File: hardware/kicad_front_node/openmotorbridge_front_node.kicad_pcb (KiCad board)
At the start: 2 copper layers, 82 x 50 mm, 54 parts, among them J1 12V_KL15_GND, J10 12V_QI_POWER, J11 12V_AUX_LIGHT, J12 QWIIC_I2C, J2 CAN_H_L_GND, J3 HANDLEBAR_MULTI_BTN, J4 USB_UPSTREAM_HOST, J5 USB_DN1_PHONE_PD20W, J5_MP3 USB_DN3_GLOVEBOX_PD20W, J6 USB_DN2_CP2AA_PIGTAIL, J6_AUX USB_DN4_COCKPIT_AUX, J7 USB-C_SERVICE, J8 ACTION_CAM_5V_PWR, J9 MIRROR_BSD_LEDS, K1 CPC1017N_CAN_RELAY, Q1 DMN63D8_BSD_MOSFET, Q2 TPS1H100_AUX_LIGHT, SW1 BOOT, SW2 RESET, U1 ESP32-S3-WROOM-1U, U2 USB2514Bi-AEZG, U3 TPS54302_5V_BUCK, U4 TPS2051B_PORT2_GATE, U5 SW3526_USB_PD1_20W, U6 TCAN334G_CAN, U7 TLV75533P_3V3_LDO, U8 SW3526_USB_PD3_20W, Y1 24.000MHz

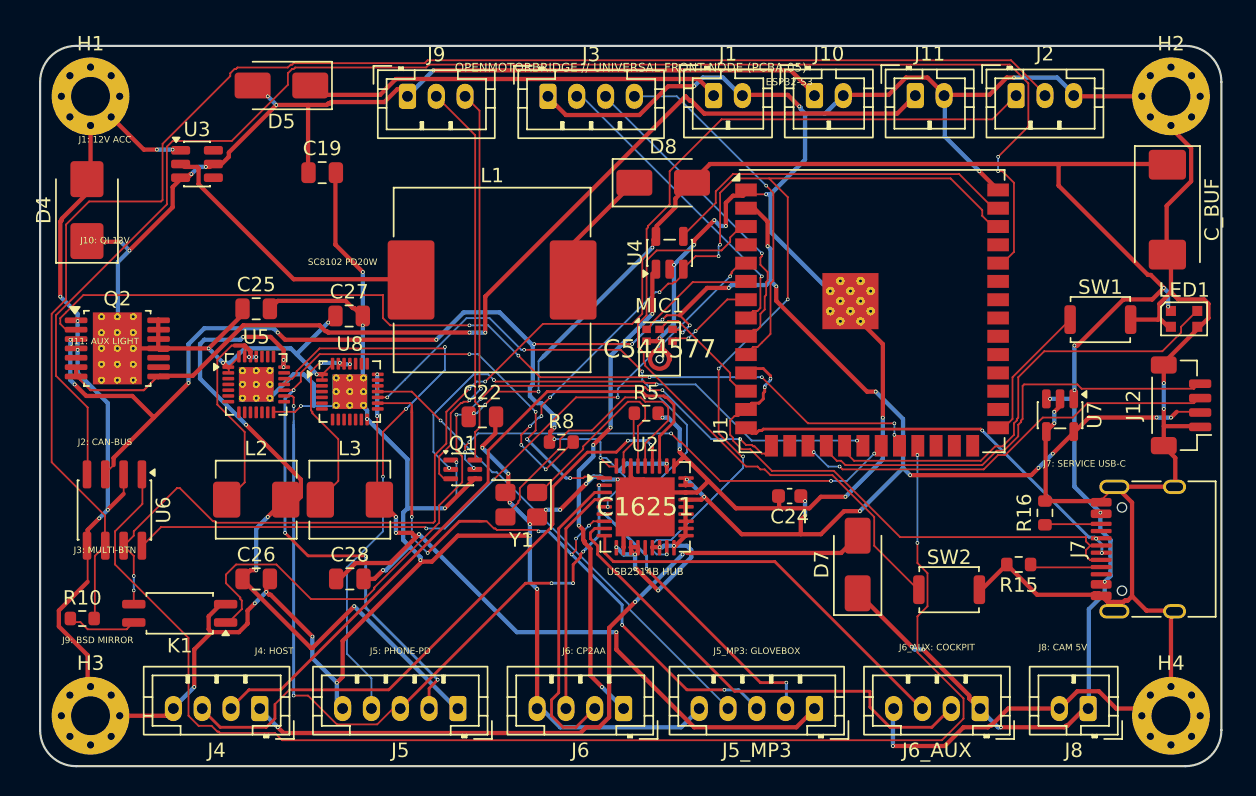
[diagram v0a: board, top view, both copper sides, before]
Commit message: hardware(pcb): mathematically align edge connectors on Front Node (PCBA 05) and Pod Cartridge (PCBA 03)
- Front Node top edge: align J1, J10, J11, J2, J3, J9 to consistent Y=73.500 (fixing 50µm step) and harmonize J9-J3 clearance to 1.60 mm
- Front Node bottom edge: adjust J5 and J6 by 0.25 mm so all 6 USB/cam ports have exactly 1.600 mm clearance
- Front Node right edge: smooth J7 USB-C service port to clean 0.5 mm grid at Y=105.000
- Pod Cartridge: smooth J_ACT to X=132.000 (3.00 mm distance to edge)
- Add inspect_and_align_pcb_connectors.py diagnostic and alignment tool
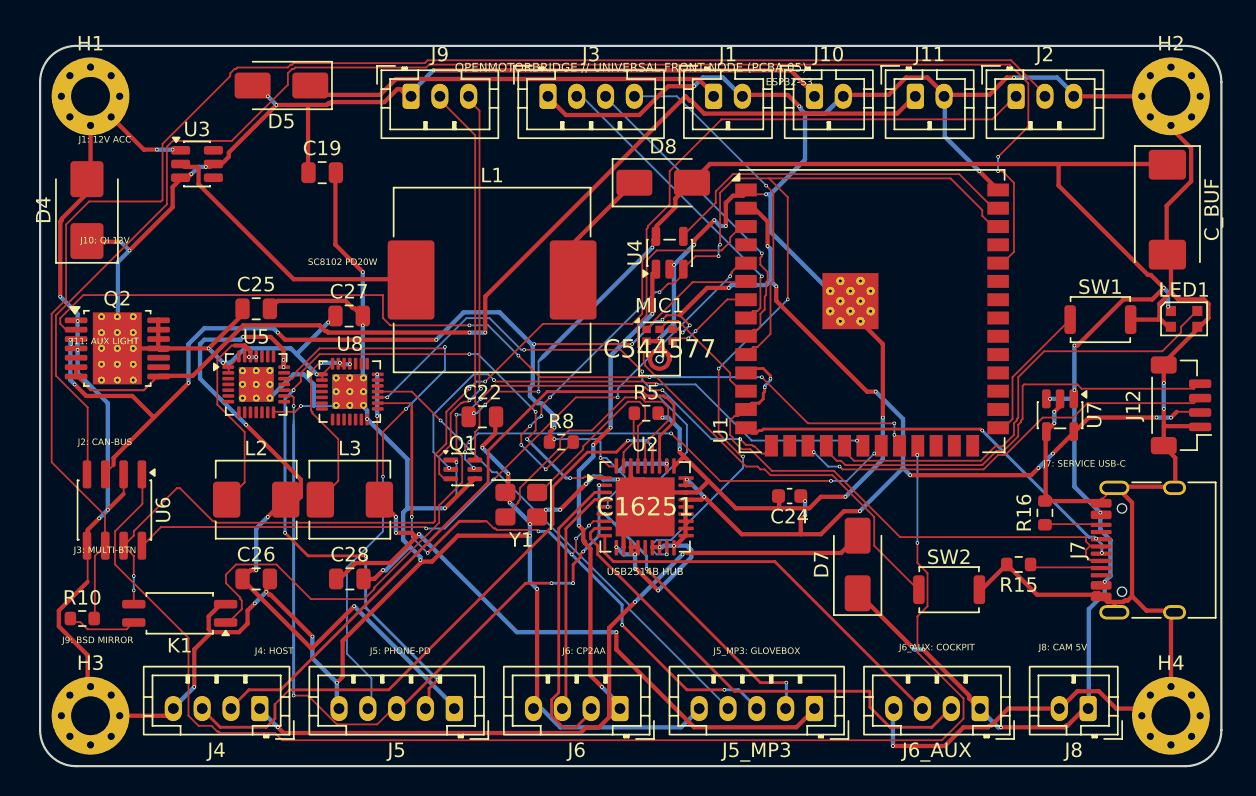
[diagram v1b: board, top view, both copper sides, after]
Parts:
- moved J5 0.25 mm to (128.8, 116.0)
- moved J6 0.25 mm to (140.2, 116.0)
- moved J9 0.25 mm to (125.8, 73.5)
- moved J7 0.07 mm to (177.7, 105.0)
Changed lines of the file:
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@@
 	(footprint "JST_PH_B5B-PH-K_1x05_P2.00mm_Vertical"
 		(layer "F.Cu")
-		(at 129 116 180)
+		(at 128.750 116.000 180.0)
 		(descr "JST PH series connector, B5B-PH-K (http://www.jst-mfg.com/product/pdf/eng/ePH.pdf)")
 		(tags "connector JST PH vertical")
@@
 	(footprint "JST_PH_B2B-PH-K_1x02_P2.00mm_Vertical"
 		(layer "F.Cu")
-		(at 153.75 73.45)
+		(at 153.750 73.500)
 		(descr "JST PH series connector, B2B-PH-K (http://www.jst-mfg.com/product/pdf/eng/ePH.pdf)")
 		(tags "connector JST PH vertical")
@@
 	(footprint "JST_PH_B3B-PH-K_1x03_P2.00mm_Vertical"
 		(layer "F.Cu")
-		(at 125.5 73.5)
+		(at 125.750 73.500)
 		(descr "JST PH series connector, B3B-PH-K (http://www.jst-mfg.com/product/pdf/eng/ePH.pdf)")
 		(tags "connector JST PH vertical")
@@
 	(footprint "JST_PH_B2B-PH-K_1x02_P2.00mm_Vertical"
 		(layer "F.Cu")
-		(at 146.75 73.45)
+		(at 146.750 73.500)
 		(descr "JST PH series connector, B2B-PH-K (http://www.jst-mfg.com/product/pdf/eng/ePH.pdf)")
 		(tags "connector JST PH vertical")
@@
 	(footprint "JST_PH_B2B-PH-K_1x02_P2.00mm_Vertical"
 		(layer "F.Cu")
-		(at 160.75 73.45)
+		(at 160.750 73.500)
 		(descr "JST PH series connector, B2B-PH-K (http://www.jst-mfg.com/product/pdf/eng/ePH.pdf)")
 		(tags "connector JST PH vertical")
@@
 	(footprint "JST_PH_B4B-PH-K_1x04_P2.00mm_Vertical"
 		(layer "F.Cu")
-		(at 140.5 116 180)
+		(at 140.250 116.000 180.0)
 		(descr "JST PH series connector, B4B-PH-K (http://www.jst-mfg.com/product/pdf/eng/ePH.pdf)")
 		(tags "connector JST PH vertical")
@@
 	(footprint "USB_C_Receptacle_HRO_TYPE-C-31-M-12"
 		(layer "F.Cu")
-		(at 177.7 104.93 90)
+		(at 177.700 105.000 90.0)
 		(descr "USB Type-C receptacle for USB 2.0 and PD, http://www.krhro.com/uploads/soft/180320/1-1P320120243.pdf")
 		(tags "usb usb-c 2.0 pd")
@@
 	(footprint "JST_PH_B3B-PH-K_1x03_P2.00mm_Vertical"
 		(layer "F.Cu")
-		(at 167.75 73.45)
+		(at 167.750 73.500)
 		(descr "JST PH series connector, B3B-PH-K (http://www.jst-mfg.com/product/pdf/eng/ePH.pdf)")
 		(tags "connector JST PH vertical")

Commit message: hardware(pcb): synchronize 5-PCBA lineup with v9.6 All-UWB architecture
- PCBA 01 (Central Box): replace obsolete 26-pin IDC header with 12-pin Deutsch DTM-12 header (exact 12-pin net mapping), add 38.4MHz UWB crystal on B.Cu, update silkscreen and schematic
- PCBA 05 (Front Node): place Qorvo DW3110 + U.FL + crystal on B.Cu; place u-blox SAM-M10Q GNSS + Knowles MEMS mic on F.Cu
- PCBA 03 (Pod Cartridge): replace obsolete 6-pin dock socket with PAD1/PAD2 DC spring contact pads; place DW3110 + U.FL on B.Cu
- PCBA 08 (Radar Sub-MCU): update J1 to 2-pin 12V automotive power connector; place DW3110 + U.FL on B.Cu
- PCBA 07 (Smart Keyfob): replace solder pads with 2-pin JST-ACH SMD header (J_QI) for solderless Qi coil connection
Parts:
- added ANT_UWB: Taoglas_FXUWB10, Connector_Coaxial:U.FL_Hirose_U.FL-R-SMT-1_Vertical, B.Cu at (137.0, 95.0)
- added MK1: SPH0645LM4H, Sensor_Audio:Knowles_SPH0645LM4H, F.Cu at (175.0, 85.0)
- added U10: u-blox_SAM-M10Q, RF_GPS:ublox_SAM-M10Q, F.Cu at (125.0, 85.0)
- added U9: DW3110, Package_DFN_QFN:QFN-16-1EP_3x3mm_P0.5mm_EP1.7x1.7mm_ThermalVias, B.Cu at (145.0, 95.0)
- added Y_UWB: 38.4MHz, Crystal:Crystal_SMD_2016-4Pin_2.0x1.6mm, B.Cu at (151.0, 95.0)
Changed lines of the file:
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@@
 	)
 	(embedded_fonts no)
+	(footprint "Package_DFN_QFN:QFN-16-1EP_3x3mm_P0.5mm_EP1.7x1.7mm_ThermalVias"
+		(layer "B.Cu")
+		(at 145 95 180)
+		(descr "Qorvo DW3110 Ultra-Wideband Transceiver")
+		(property "Reference" "U9"
+			(at 0 -2.5 0)
+			(layer "B.SilkS")
+			(effects
+				(font
+					(size 0.8 0.8)
+					(thickness 0.12)
+				)
+				(justify mirror)
+			)
+		)
+		(property "Value" "DW3110"
+			(at 0 2.5 0)
+			(layer "B.Fab")
+			(effects
+				(font
+					(size 0.8 0.8)
+					(thickness 0.12)
+				)
+				(justify mirror)
+			)
+		)
+		(pad "1" smd roundrect (at -1.45 0.75 180) (size 0.6 0.25) (layers "B.Cu" "B.Mask" "B.Paste") (roundrect_rratio 0.25))
+		(pad "2" smd roundrect (at -1.45 0.25 180) (size 0.6 0.25) (layers "B.Cu" "B.Mask" "B.Paste") (roundrect_rratio 0.25))
+		(pad "3" smd roundrect (at -1.45 -0.25 180) (size 0.6 0.25) (layers "B.Cu" "B.Mask" "B.Paste") (roundrect_rratio 0.25))
+		(pad "4" smd roundrect (at -1.45 -0.75 180) (size 0.6 0.25) (layers "B.Cu" "B.Mask" "B.Paste") (roundrect_rratio 0.25))
+		(pad "5" smd roundrect (at -0.75 -1.45 180) (size 0.25 0.6) (layers "B.Cu" "B.Mask" "B.Paste") (roundrect_rratio 0.25))
+		(pad "6" smd roundrect (at -0.25 -1.45 180) (size 0.25 0.6) (layers "B.Cu" "B.Mask" "B.Paste") (roundrect_rratio 0.25))
+		(pad "7" smd roundrect (at 0.25 -1.45 180) (size 0.25 0.6) (layers "B.Cu" "B.Mask" "B.Paste") (roundrect_rratio 0.25))
+		(pad "8" smd roundrect (at 0.75 -1.45 180) (size 0.25 0.6) (layers "B.Cu" "B.Mask" "B.Paste") (roundrect_rratio 0.25))
+		(pad "9" smd roundrect (at 1.45 -0.75 180) (size 0.6 0.25) (layers "B.Cu" "B.Mask" "B.Paste") (roundrect_rratio 0.25))
+		(pad "10" smd roundrect (at 1.45 -0.25 180) (size 0.6 0.25) (layers "B.Cu" "B.Mask" "B.Paste") (roundrect_rratio 0.25))
+		(pad "11" smd roundrect (at 1.45 0.25 180) (size 0.6 0.25) (layers "B.Cu" "B.Mask" "B.Paste") (roundrect_rratio 0.25))
+		(pad "12" smd roundrect (at 1.45 0.75 180) (size 0.6 0.25) (layers "B.Cu" "B.Mask" "B.Paste") (roundrect_rratio 0.25))
+		(pad "13" smd roundrect (at 0.75 1.45 180) (size 0.25 0.6) (layers "B.Cu" "B.Mask" "B.Paste") (roundrect_rratio 0.25))
+		(pad "14" smd roundrect (at 0.25 1.45 180) (size 0.25 0.6) (layers "B.Cu" "B.Mask" "B.Paste") (roundrect_rratio 0.25))
+		(pad "15" smd roundrect (at -0.25 1.45 180) (size 0.25 0.6) (layers "B.Cu" "B.Mask" "B.Paste") (roundrect_rratio 0.25))
+		(pad "16" smd roundrect (at -0.75 1.45 180) (size 0.25 0.6) (layers "B.Cu" "B.Mask" "B.Paste") (roundrect_rratio 0.25))
+		(pad "17" smd roundrect (at 0 0 180) (size 1.7 1.7) (layers "B.Cu" "B.Mask" "B.Paste") (roundrect_rratio 0.1) (net "GND"))
+	)
+	(footprint "Connector_Coaxial:U.FL_Hirose_U.FL-R-SMT-1_Vertical"
+		(layer "B.Cu")
+		(at 137 95 180)
+		(descr "Hirose U.FL Coaxial Connector (Taoglas FXUWB10 Floor Antenna)")
+		(property "Reference" "ANT_UWB"
+			(at 0 -2.5 0)
+			(layer "B.SilkS")
+			(effects
+				(font
+					(size 0.8 0.8)
+					(thickness 0.12)
+				)
+				(justify mirror)
+			)
+		)
+		(property "Value" "Taoglas_FXUWB10"
+			(at 0 2.5 0)
+			(layer "B.Fab")
+			(effects
+				(font
+					(size 0.8 0.8)
+					(thickness 0.12)
+				)
+				(justify mirror)
+			)
+		)
+		(pad "1" smd roundrect (at 0 -1.5 180) (size 1.0 1.0) (layers "B.Cu" "B.Mask" "B.Paste") (roundrect_rratio 0.25))
+		(pad "2" smd roundrect (at -1.05 0 180) (size 0.8 1.1) (layers "B.Cu" "B.Mask" "B.Paste") (roundrect_rratio 0.25) (net "GND"))
+		(pad "2" smd roundrect (at 1.05 0 180) (size 0.8 1.1) (layers "B.Cu" "B.Mask" "B.Paste") (roundrect_rratio 0.25) (net "GND"))
+	)
+	(footprint "Crystal:Crystal_SMD_2016-4Pin_2.0x1.6mm"
+		(layer "B.Cu")
+		(at 151 95 180)
+		(descr "SMD Crystal 38.4MHz 2.0x1.6mm 4-Pin")
+		(property "Reference" "Y_UWB"
+			(at 0 -1.5 0)
+			(layer "B.SilkS")
+			(effects
+				(font
+					(size 0.7 0.7)
+					(thickness 0.12)
+				)
+				(justify mirror)
+			)
+		)
+		(property "Value" "38.4MHz"
+			(at 0 1.5 0)
+			(layer "B.Fab")
+			(effects
+				(font
+					(size 0.7 0.7)
+					(thickness 0.12)
+				)
+				(justify mirror)
+			)
+		)
+		(pad "1" smd roundrect (at -0.65 0.5 180) (size 0.7 0.6) (layers "B.Cu" "B.Mask" "B.Paste") (roundrect_rratio 0.25))
+		(pad "2" smd roundrect (at 0.65 0.5 180) (size 0.7 0.6) (layers "B.Cu" "B.Mask" "B.Paste") (roundrect_rratio 0.25) (net "GND"))
+		(pad "3" smd roundrect (at 0.65 -0.5 180) (size 0.7 0.6) (layers "B.Cu" "B.Mask" "B.Paste") (roundrect_rratio 0.25))
+		(pad "4" smd roundrect (at -0.65 -0.5 180) (size 0.7 0.6) (layers "B.Cu" "B.Mask" "B.Paste") (roundrect_rratio 0.25) (net "GND"))
+	)
+	(footprint "RF_GPS:ublox_SAM-M10Q"
+		(layer "F.Cu")
+		(at 125 85 0)
+		(descr "u-blox SAM-M10Q Standard Precision GNSS Module with Integrated Patch Antenna (15.5x15.5mm)")
+		(property "Reference" "U10"
+			(at 0 -9.0 0)
+			(layer "F.SilkS")
+			(effects
+				(font
+					(size 0.8 0.8)
+					(thickness 0.12)
+				)
+			)
+		)
+		(property "Value" "u-blox_SAM-M10Q"
+			(at 0 9.0 0)
+			(layer "F.Fab")
+			(effects
+				(font
+					(size 0.8 0.8)
+					(thickness 0.12)
+				)
+			)
+		)
+		(fp_rect (start -7.75 -7.75) (end 7.75 7.75) (stroke (width 0.15) (type solid)) (fill no) (layer "F.SilkS"))
+		(pad "1" smd roundrect (at -6.75 -5.0) (size 1.2 0.8) (layers "F.Cu" "F.Mask" "F.Paste") (roundrect_rratio 0.25) (net "GND"))
+		(pad "2" smd roundrect (at -6.75 -2.5) (size 1.2 0.8) (layers "F.Cu" "F.Mask" "F.Paste") (roundrect_rratio 0.25) (net "3V3"))
+		(pad "3" smd roundrect (at -6.75 0.0) (size 1.2 0.8) (layers "F.Cu" "F.Mask" "F.Paste") (roundrect_rratio 0.25))
+		(pad "4" smd roundrect (at -6.75 2.5) (size 1.2 0.8) (layers "F.Cu" "F.Mask" "F.Paste") (roundrect_rratio 0.25))
+		(pad "5" smd roundrect (at -6.75 5.0) (size 1.2 0.8) (layers "F.Cu" "F.Mask" "F.Paste") (roundrect_rratio 0.25) (net "GND"))
+		(pad "6" smd roundrect (at 6.75 5.0) (size 1.2 0.8) (layers "F.Cu" "F.Mask" "F.Paste") (roundrect_rratio 0.25) (net "GND"))
+		(pad "7" smd roundrect (at 6.75 2.5) (size 1.2 0.8) (layers "F.Cu" "F.Mask" "F.Paste") (roundrect_rratio 0.25))
+		(pad "8" smd roundrect (at 6.75 0.0) (size 1.2 0.8) (layers "F.Cu" "F.Mask" "F.Paste") (roundrect_rratio 0.25))
+		(pad "9" smd roundrect (at 6.75 -2.5) (size 1.2 0.8) (layers "F.Cu" "F.Mask" "F.Paste") (roundrect_rratio 0.25) (net "3V3"))
+		(pad "10" smd roundrect (at 6.75 -5.0) (size 1.2 0.8) (layers "F.Cu" "F.Mask" "F.Paste") (roundrect_rratio 0.25) (net "GND"))
+	)
+	(footprint "Sensor_Audio:Knowles_SPH0645LM4H"
+		(layer "F.Cu")
+		(at 175 85 0)
+		(descr "Knowles SPH0645LM4H I2S MEMS Microphone")
+		(property "Reference" "MK1"
+			(at 0 -2.5 0)
+			(layer "F.SilkS")
+			(effects
+				(font
+					(size 0.7 0.7)
+					(thickness 0.12)
+				)
+			)
+		)
+		(property "Value" "SPH0645LM4H"
+			(at 0 2.5 0)
+			(layer "F.Fab")
+			(effects
+				(font
+					(size 0.7 0.7)
+					(thickness 0.12)
+				)
+			)
+		)
+		(pad "1" smd circle (at -0.8 -0.8) (size 0.5 0.5) (layers "F.Cu" "F.Mask" "F.Paste"))
+		(pad "2" smd circle (at 0.8 -0.8) (size 0.5 0.5) (layers "F.Cu" "F.Mask" "F.Paste"))
+		(pad "3" smd circle (at 0.8 0.8) (size 0.5 0.5) (layers "F.Cu" "F.Mask" "F.Paste"))
+		(pad "4" smd circle (at -0.8 0.8) (size 0.5 0.5) (layers "F.Cu" "F.Mask" "F.Paste"))
+		(pad "5" smd circle (at 0 0) (size 0.8 0.8) (layers "F.Cu" "F.Mask" "F.Paste") (net "GND"))
+	)
 )

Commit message: hardware(front-node): remove misplaced onboard ublox SAM-M10Q footprint; cluster connects externally via J12 Qwiic
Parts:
- removed U10: u-blox_SAM-M10Q, RF_GPS:ublox_SAM-M10Q
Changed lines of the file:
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@@
 		(embedded_fonts no)
-	)
-	(footprint "RF_GPS:ublox_SAM-M10Q"
-		(layer "F.Cu")
-		(at 125 85)
-		(descr "u-blox SAM-M10Q Standard Precision GNSS Module with Integrated Patch Antenna (15.5x15.5mm)")
-		(property "Reference" "U10"
-			(at 0 -9 0)
-			(layer "F.SilkS")
-			(effects
-				(font
-					(size 0.8 0.8)
-					(thickness 0.12)
-				)
-			)
-		)
-		(property "Value" "u-blox_SAM-M10Q"
-			(at 0 9 0)
-			(layer "F.Fab")
-			(effects
-				(font
-					(size 0.8 0.8)
-					(thickness 0.12)
-				)
-			)
-		)
-		(property "Datasheet" ""
-			(at 0 0 0)
-			(layer "F.Fab")
-			(hide yes)
-			(effects
-				(font
-					(size 1.27 1.27)
-				)
-			)
-		)
-		(property "Description" ""
-			(at 0 0 0)
-			(layer "F.Fab")
-			(hide yes)
-			(effects
-				(font
-					(size 1.27 1.27)
-				)
-			)
-		)
-		(duplicate_pad_numbers_are_jumpers no)
-		(fp_rect
-			(start -7.75 -7.75)
-			(end 7.75 7.75)
-			(stroke
-				(width 0.15)
-				(type solid)
-			)
-			(fill no)
-			(layer "F.SilkS")
-		)
-		(pad "1" smd roundrect
-			(at -6.75 -5)
-			(size 1.2 0.8)
-			(layers "F.Cu" "F.Mask" "F.Paste")
-			(roundrect_rratio 0.25)
-			(net "GND")
-		)
-		(pad "2" smd roundrect
-			(at -6.75 -2.5)
-			(size 1.2 0.8)
-			(layers "F.Cu" "F.Mask" "F.Paste")
-			(roundrect_rratio 0.25)
-			(net "3V3")
-		)
-		(pad "3" smd roundrect
-			(at -6.75 0)
-			(size 1.2 0.8)
-			(layers "F.Cu" "F.Mask" "F.Paste")
-			(roundrect_rratio 0.25)
-		)
-		(pad "4" smd roundrect
-			(at -6.75 2.5)
-			(size 1.2 0.8)
-			(layers "F.Cu" "F.Mask" "F.Paste")
-			(roundrect_rratio 0.25)
-		)
-		(pad "5" smd roundrect
-			(at -6.75 5)
-			(size 1.2 0.8)
-			(layers "F.Cu" "F.Mask" "F.Paste")
-			(roundrect_rratio 0.25)
-			(net "GND")
-		)
-		(pad "6" smd roundrect
-			(at 6.75 5)
-			(size 1.2 0.8)
-			(layers "F.Cu" "F.Mask" "F.Paste")
-			(roundrect_rratio 0.25)
-			(net "GND")
-		)
-		(pad "7" smd roundrect
-			(at 6.75 2.5)
-			(size 1.2 0.8)
-			(layers "F.Cu" "F.Mask" "F.Paste")
-			(roundrect_rratio 0.25)
-		)
-		(pad "8" smd roundrect
-			(at 6.75 0)
-			(size 1.2 0.8)
-			(layers "F.Cu" "F.Mask" "F.Paste")
-			(roundrect_rratio 0.25)
-		)
-		(pad "9" smd roundrect
-			(at 6.75 -2.5)
-			(size 1.2 0.8)
-			(layers "F.Cu" "F.Mask" "F.Paste")
-			(roundrect_rratio 0.25)
-			(net "3V3")
-		)
-		(pad "10" smd roundrect
-			(at 6.75 -5)
-			(size 1.2 0.8)
-			(layers "F.Cu" "F.Mask" "F.Paste")
-			(roundrect_rratio 0.25)
-			(net "GND")
-		)
-		(embedded_fonts no)
-		(model "${KICAD10_3DMODEL_DIR}/RF_Module.3dshapes/Raytac_MDBT50Q.step"
-			(offset
-				(xyz 0 0 0)
-			)
-			(scale
-				(xyz 1.4 0.9 1.8)
-			)
-			(rotate
-				(xyz 0 0 0)
-			)
-		)
 	)
 	(footprint "L_Sunlord_MWSA0503S"
